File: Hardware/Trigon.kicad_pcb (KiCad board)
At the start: 2 copper layers, 160 x 120 mm, 110 parts, among them J1 TYPE-C-31-M12_13, J2 TYPE-C-31-M12_13, J3 Conn_01x05, SW1 SW_Push, SW2 Rotary_Encoder_Switch, U1 ATmega32U4-AU, U2 USBLC6-2SC6, U3 CY7C65632-28LTXCT, U4 USBLC6-2SC6, Y1 16MHz, Y2 12MHz

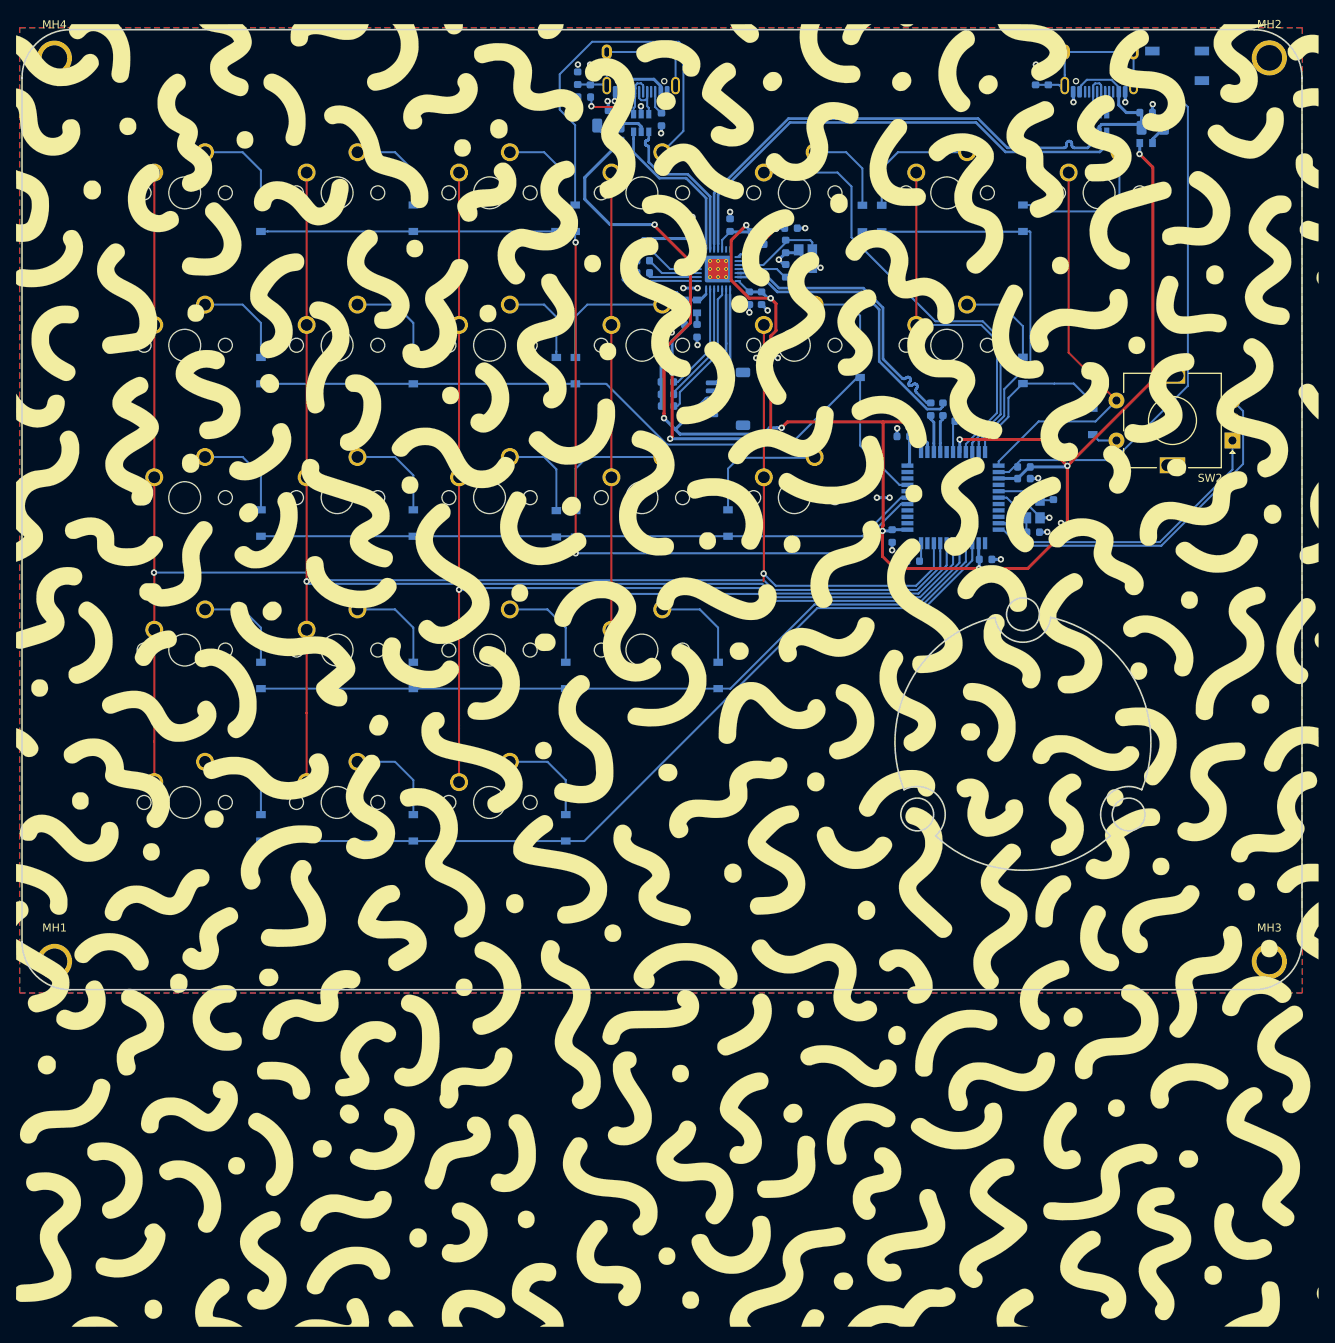
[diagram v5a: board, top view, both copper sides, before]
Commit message: kailh hotswap switches ;now using a fixed acheron
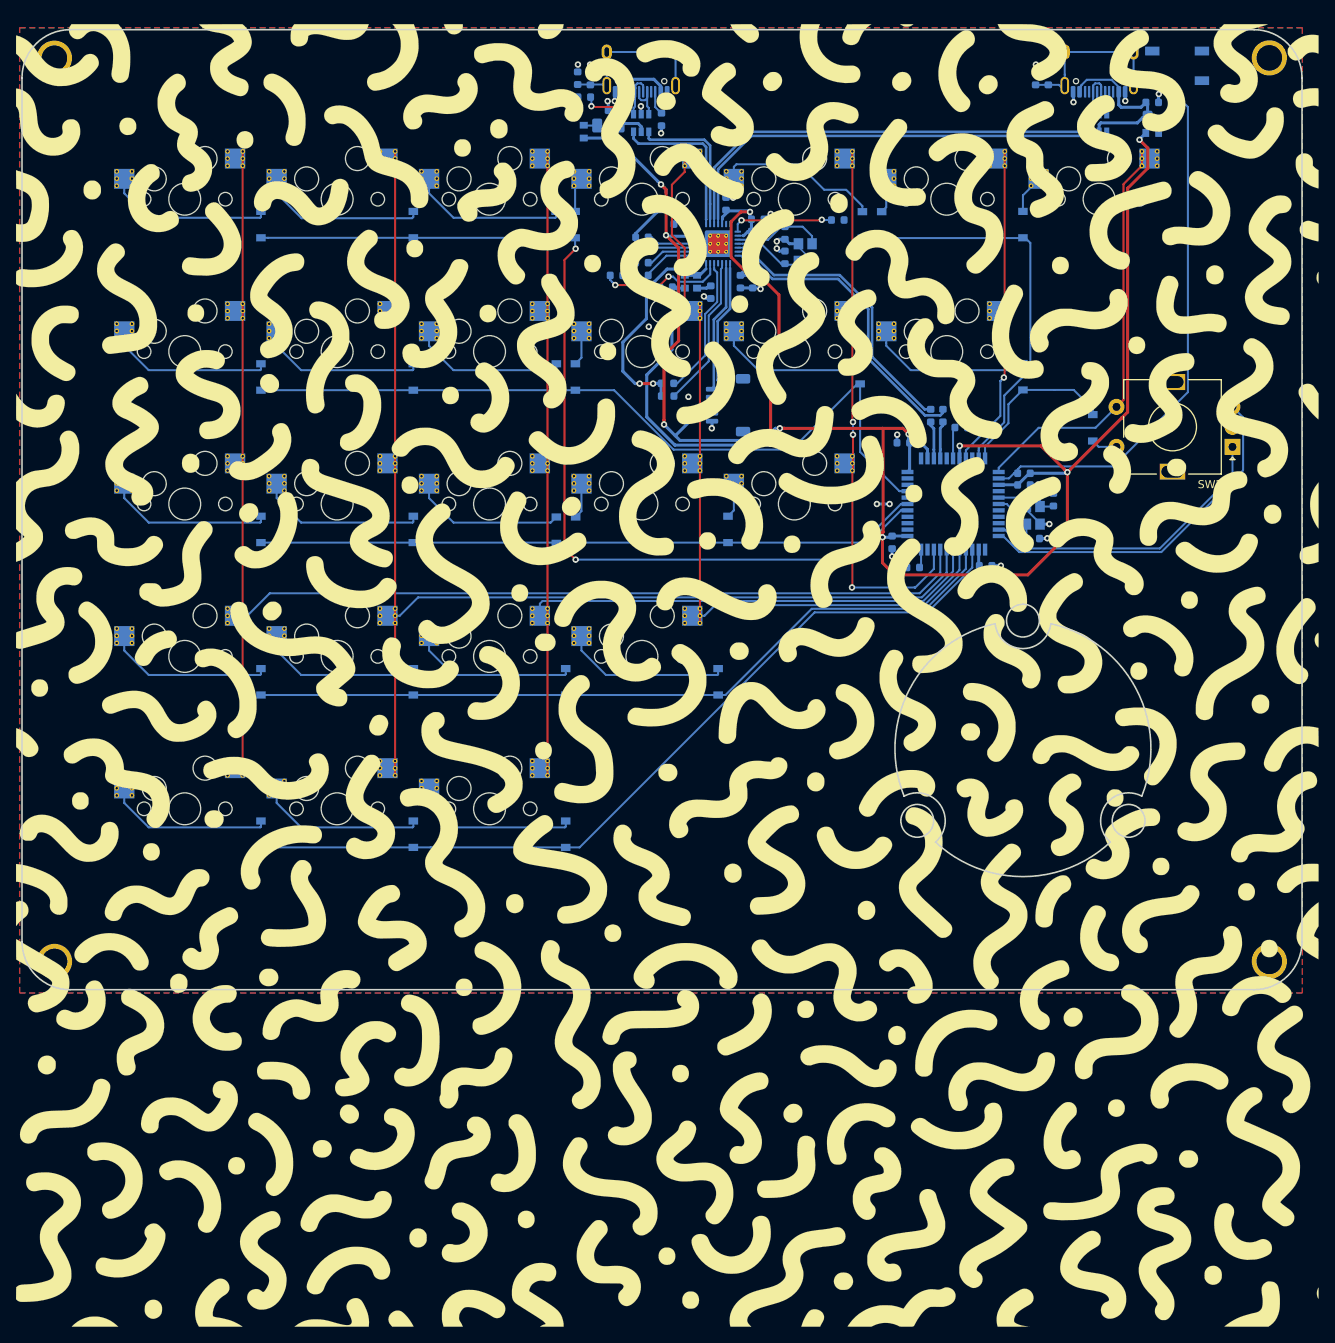
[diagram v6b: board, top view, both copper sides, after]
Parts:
- MH1, MH2, MH3, MH4: moved to B.Cu
- MX1, MX10, MX11, MX12, MX13, MX14, MX15, MX16, MX17, MX18, MX19, MX2, MX20, MX21, MX22, MX23, MX24, MX25, MX3, MX4, MX5, MX6, MX7, MX8, MX9: footprint MX_Only:MXOnly-1U-NoLED -> josh-keyboard:Kailh_Hotswap_1U; moved to B.Cu
- moved R13 14.8 mm to (86.5, 42.9), turned to 180 degrees
- moved R10 5.93 mm to (114.2, 35.9)
- moved C8 5.12 mm to (98.3, 45.0)
- moved C12 4.94 mm to (92.7, 44.3)
- moved FB4 4.01 mm to (82.4, 24.9), turned to 90 degrees
- moved U3 3.18 mm to (99.2, 38.9)
- moved FB1 3.08 mm to (96.6, 43.7)
- moved FB2 3.08 mm to (95.1, 43.7)
- moved C14 2.71 mm to (100.2, 33.9)
- moved C16 2.36 mm to (103.5, 43.6)
- moved C17 2.36 mm to (102.0, 43.6)
- moved C11 1.83 mm to (94.5, 36.4), turned to 180 degrees
- moved C10 1.69 mm to (107.6, 40.6)
- moved C9 1.69 mm to (107.6, 37.6)
- moved C13 1.59 mm to (104.2, 37.4)
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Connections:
- MX5 pad 1: COL3.5 -> COL4
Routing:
- net COL3.5: track 57.5 -> 0.00 mm
- net Net-(D4-Pad2): track 48.9 -> 5.52 mm
- net Net-(D7-Pad2): track 19.0 -> 4.88 mm
- net Net-(D18-Pad2): track 16.7 -> 4.37 mm
- net Net-(D11-Pad2): track 16.6 -> 4.38 mm
- net Net-(D17-Pad2): track 16.7 -> 4.46 mm
- net Net-(D6-Pad2): track 16.1 -> 4.33 mm
- net COL4: track 58.0 -> 68.2 mm, vias 1 -> 3
- net Net-(D5-Pad2): track 11.4 -> 20.6 mm
- net +3.3VA: track 77.8 -> 86.8 mm, vias 5 -> 3
- net Net-(D13-Pad2): track 12.0 -> 20.9 mm
- net Net-(D12-Pad2): track 10.7 -> 19.5 mm
- net Net-(D2-Pad2): track 12.3 -> 20.9 mm
- net Net-(D8-Pad2): track 12.3 -> 20.9 mm
- net Net-(D9-Pad2): track 12.3 -> 20.9 mm
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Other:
- outline, holes or cut-outs redrawn
- rule pad_to_mask_clearance: 0.051 -> 0

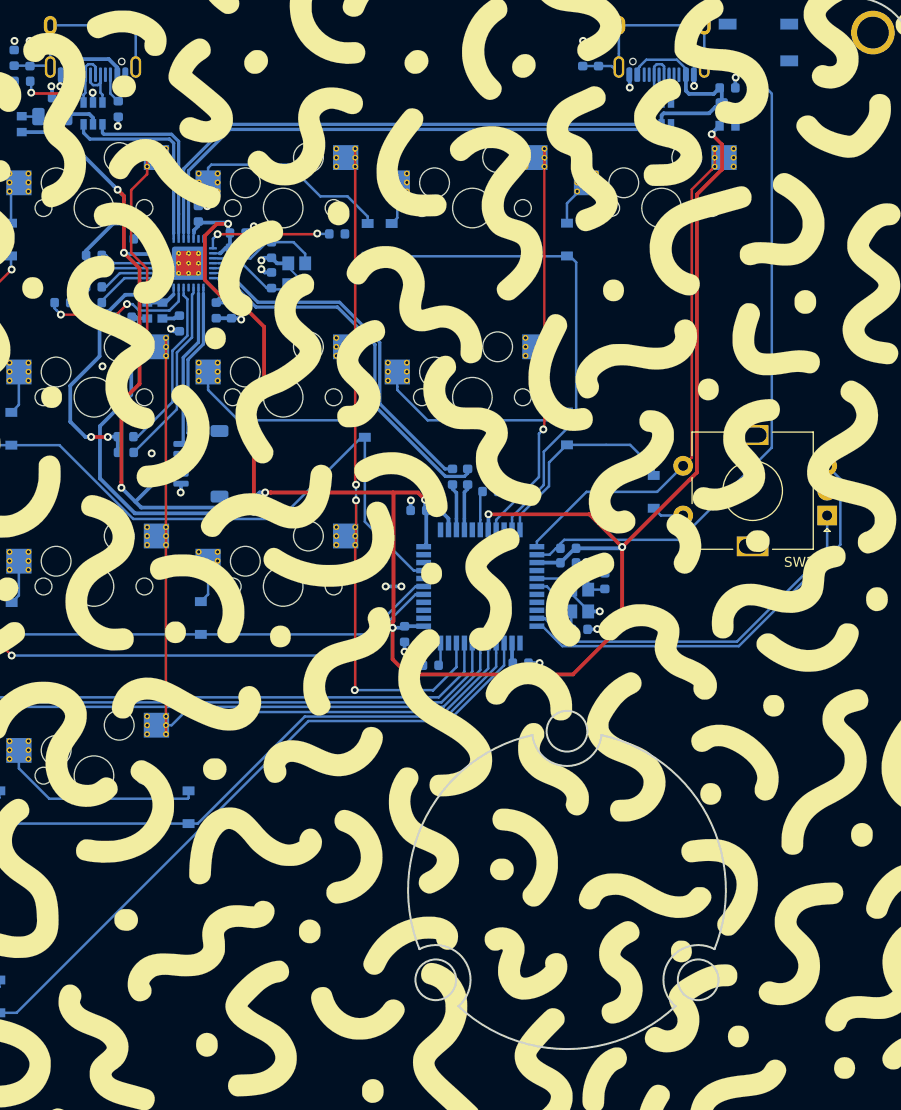
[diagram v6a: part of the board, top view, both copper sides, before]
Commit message: using hotswaps
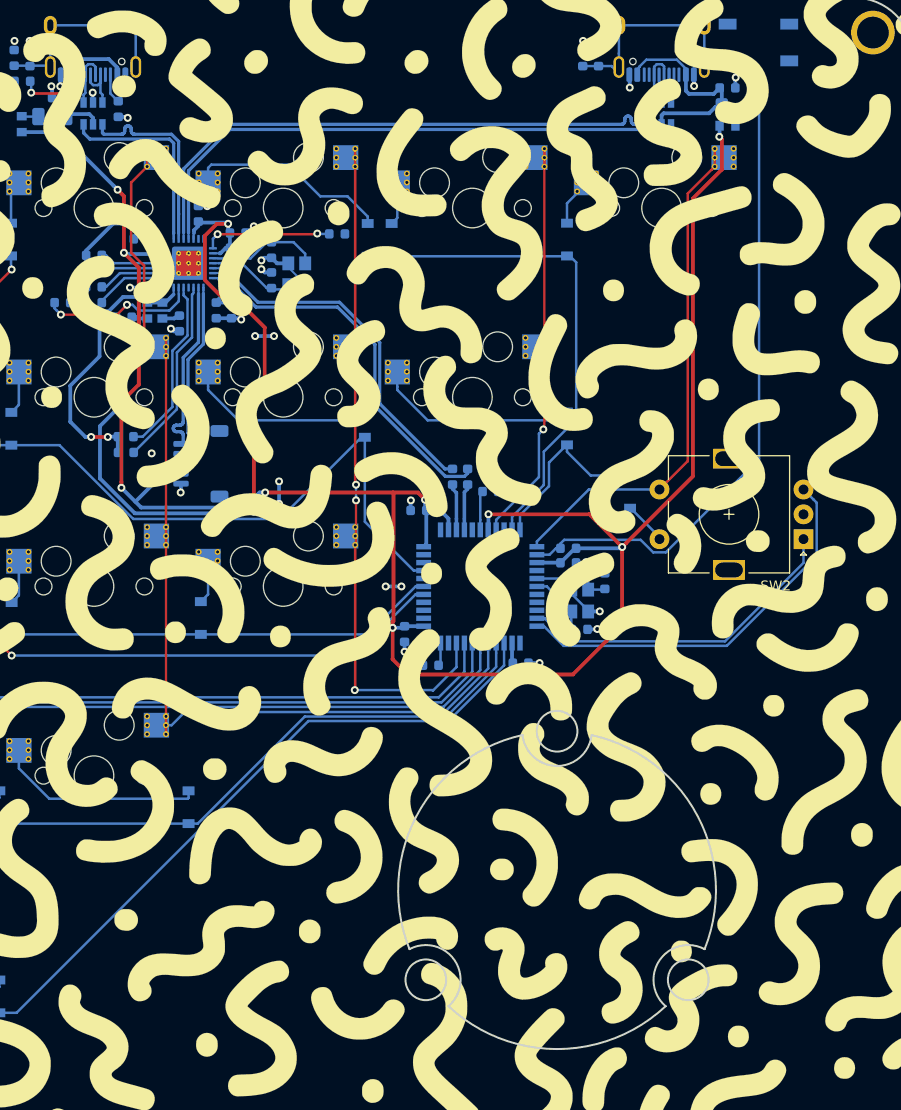
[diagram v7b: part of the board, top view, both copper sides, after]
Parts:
- moved SW2 3.37 mm to (161.1, 66.7)
- moved D26 2.38 mm to (143.7, 61.9)
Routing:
- net GND: track 47.0 -> 53.5 mm, vias 41 -> 46
- net ENC1B: track 44.1 -> 40.0 mm
- net ENC1A: track 37.6 -> 33.5 mm
- net ROW1.5: track 21.0 -> 18.6 mm
- net +5V: track 226.8 -> 224.8 mm
- net D2_D+: track 16.5 -> 17.9 mm
- net UP_D+: track 18.9 -> 20.0 mm
- net Net-(D26-Pad2): track 3.27 -> 4.38 mm
- net D1_D-: track 56.1 -> 57.2 mm
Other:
- outline, holes or cut-outs redrawn
- rule pad_to_mask_clearance: 0 -> 0.05
